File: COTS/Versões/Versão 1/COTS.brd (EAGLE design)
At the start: 76.2 x 79.7 mm, 12 parts

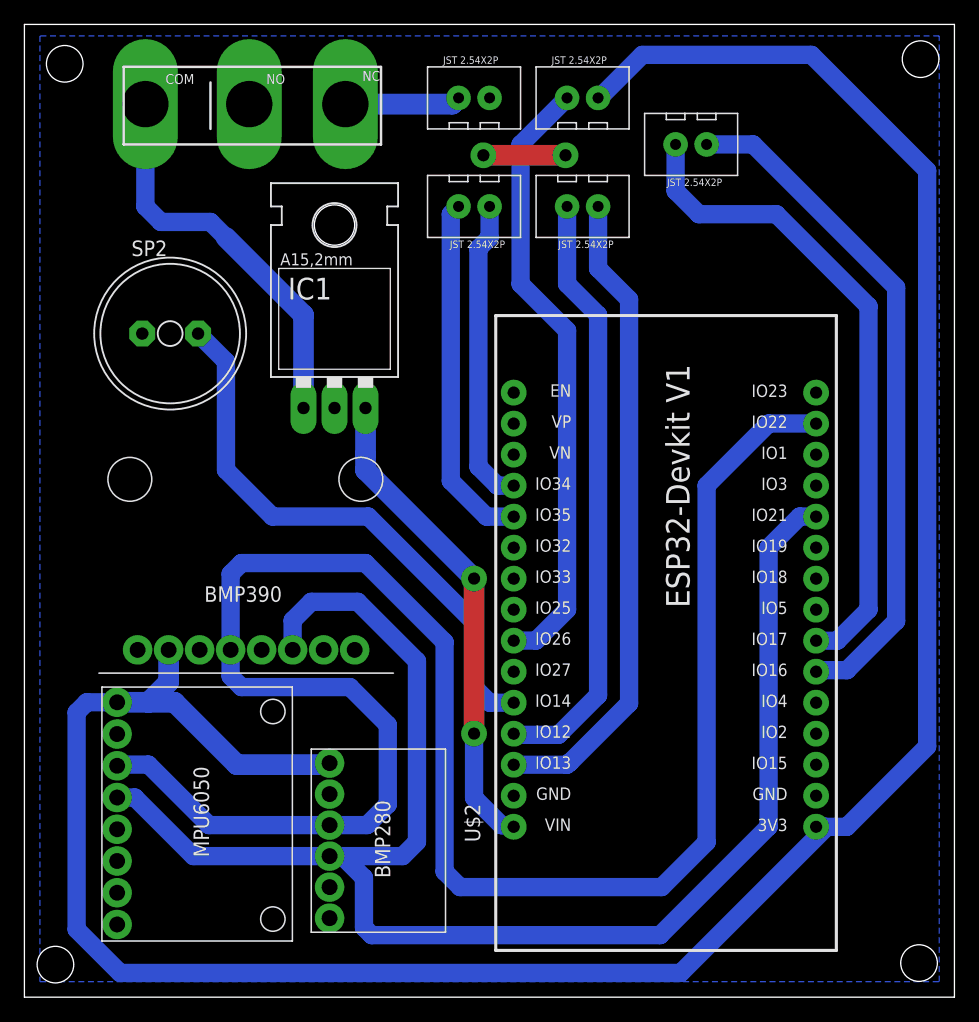
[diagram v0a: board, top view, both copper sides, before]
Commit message: CHORE: colocando  pads ovais
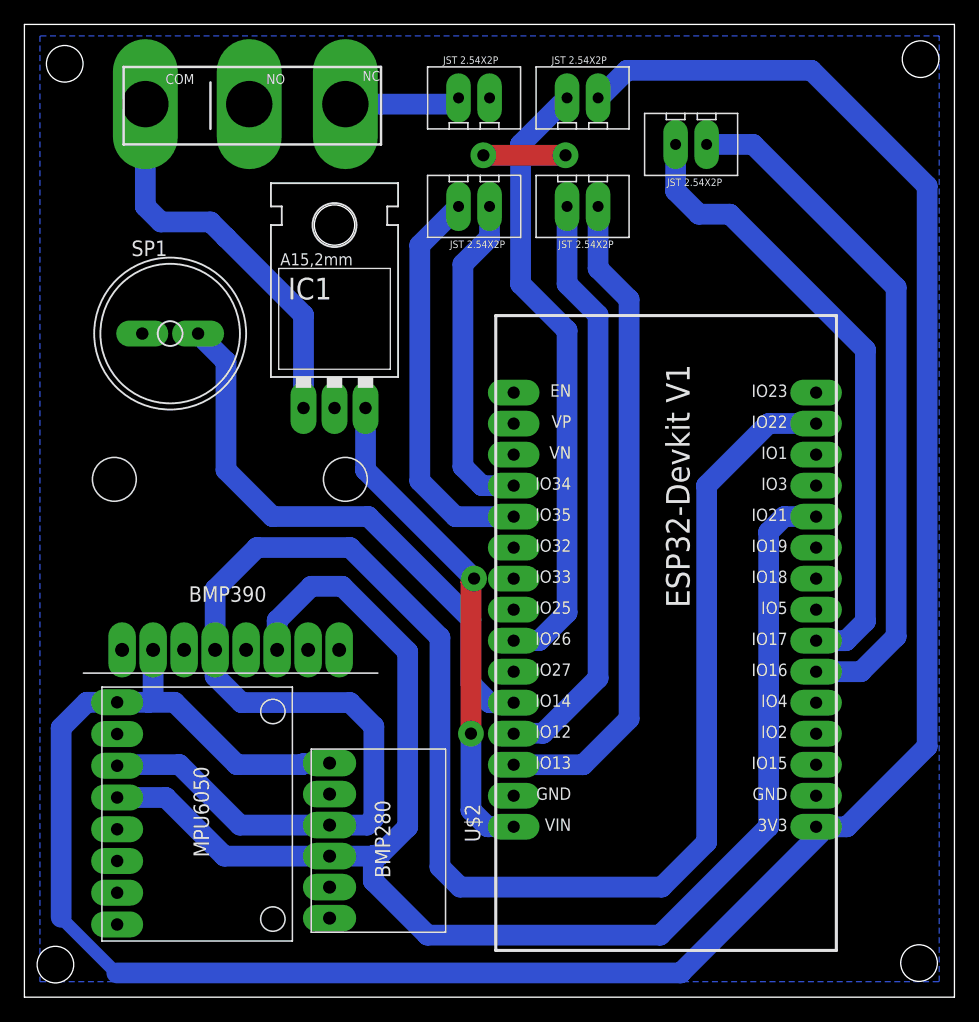
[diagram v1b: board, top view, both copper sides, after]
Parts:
- moved U$3 1.27 mm to (16.5, 36.8)
- renumbered SP2 to SP1
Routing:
- net OPTOACOPLADOR2: track 29.1 -> 32.7 mm
- net SDA: track 128.6 -> 126.1 mm
- net TX2: track 53.7 -> 51.7 mm
- net OPTOACOPLADOR1: track 25.2 -> 27.0 mm
- net SCL: track 157.6 -> 158.7 mm
- net SKIB2: track 49.6 -> 48.5 mm
- net 3V3: track 205.2 -> 204.1 mm
- net 5V: track 39.8 -> 40.8 mm
- net SKIB1: track 53.3 -> 54.0 mm
- net RX2: track 56.0 -> 56.7 mm

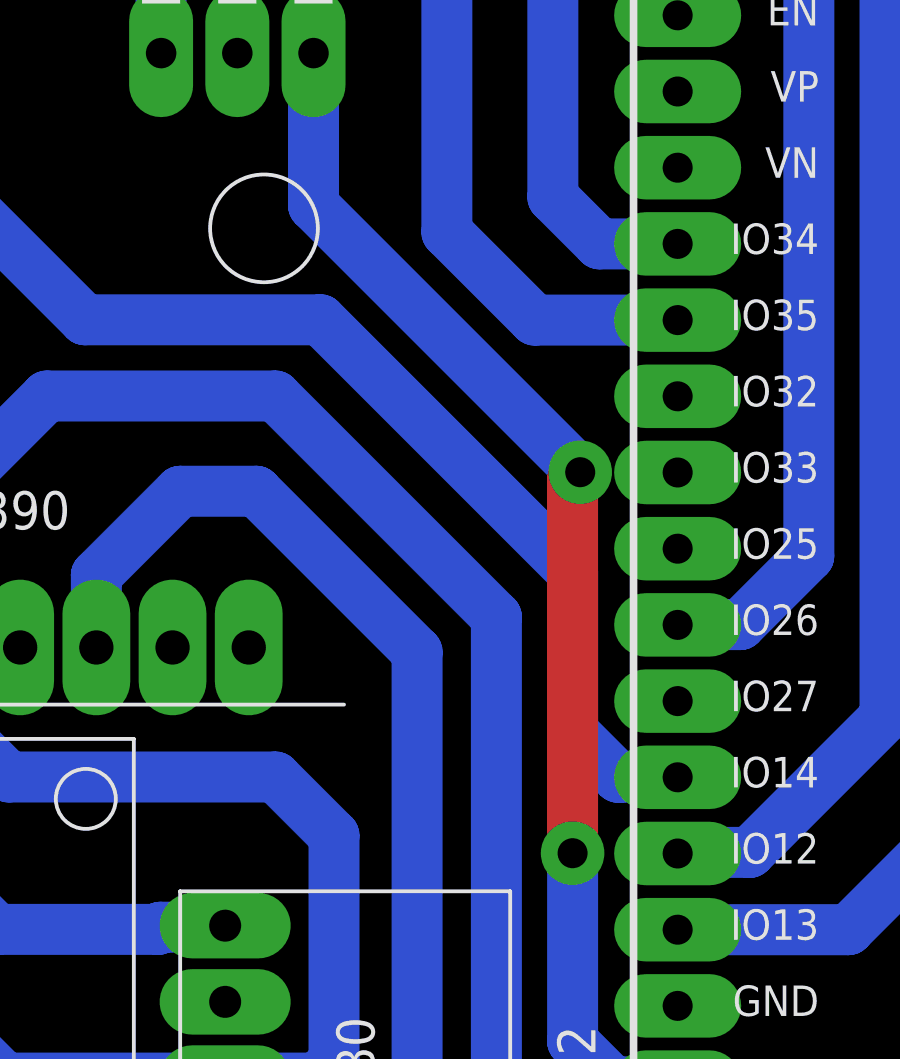
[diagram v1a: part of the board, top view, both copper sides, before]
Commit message: FIX: movendo LoRa para melhor posição
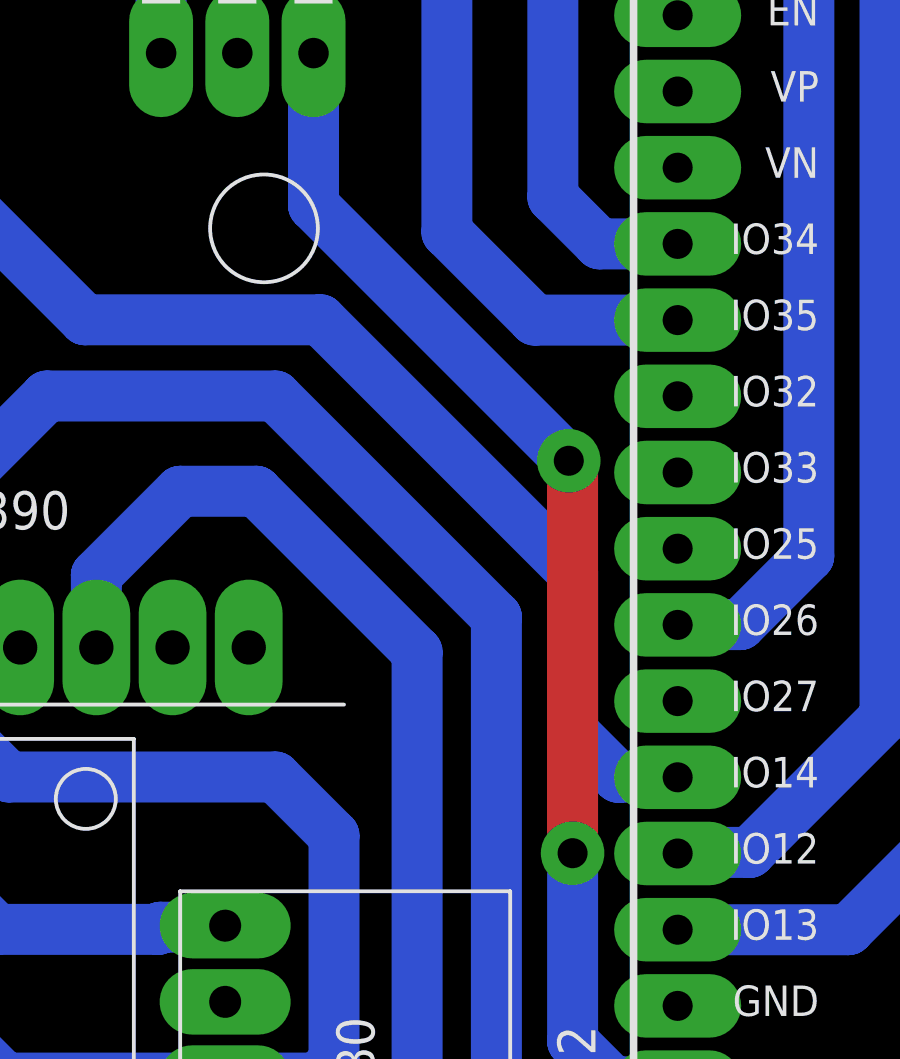
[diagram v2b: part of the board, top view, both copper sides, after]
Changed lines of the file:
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@@
 <elements>
 <element name="U$1" library="CRD" library_urn="urn:adsk.eagle:library:39051337" package="MPU6050_FOOTPRINT" package3d_urn="urn:adsk.eagle:package:39029071/10" override_package3d_urn="urn:adsk.eagle:package:49473311/2" override_package_urn="urn:adsk.eagle:footprint:39029067/6" override_locally_modified="yes" value="MPU6050V1" x="17.78" y="15.24" smashed="yes" rot="R270"/>
-<element name="U$2" library="ESP32-DEVKITV1" library_urn="urn:adsk.eagle:library:44018017" package="ESP32-DEVKITV1" package3d_urn="urn:adsk.eagle:package:44018021/2" value="ESP32DEVKITV1" x="51.308" y="36.83" smashed="yes" rot="R90">
+<element name="U$2" library="ESP32-DEVKITV1" library_urn="urn:adsk.eagle:library:44018017" package="ESP32-DEVKITV1" package3d_urn="urn:adsk.eagle:package:44018021/2" override_package3d_urn="urn:adsk.eagle:package:49887807/2" override_package_urn="urn:adsk.eagle:footprint:49887808/1" value="ESP32DEVKITV1" x="51.308" y="36.83" smashed="yes" rot="R90">
 <attribute name="NAME" x="37.338" y="12.7" size="1.27" layer="21" rot="R90"/>
 </element>
@@
 <element name="U$8" library="CRD" library_urn="urn:adsk.eagle:library:39051337" package="CHAVESS-5GL" package3d_urn="urn:adsk.eagle:package:45208058/14" value="CHAVE_SS-5GL" x="19.05" y="72.39" smashed="yes"/>
 <element name="U$10" library="CRD" library_urn="urn:adsk.eagle:library:39051337" package="BMP280_FOOTPRINT" package3d_urn="urn:adsk.eagle:package:39029072/8" value="BMP280V1" x="31.115" y="12.7" smashed="yes" rot="R270"/>
-<element name="SP1" library="buzzer" package="AL11P" package3d_urn="urn:adsk.eagle:package:5308/1" value="AL11P" x="11.938" y="54.356" smashed="yes">
+<element name="SP1" library="buzzer" package="AL11P" package3d_urn="urn:adsk.eagle:package:5308/1" override_package3d_urn="urn:adsk.eagle:package:49887804/2" override_package_urn="urn:adsk.eagle:footprint:49887805/1" value="AL11P" x="11.938" y="54.356" smashed="yes">
 <attribute name="MF" value="" x="11.938" y="54.356" size="1.778" layer="27" display="off"/>
 <attribute name="MPN" value="" x="11.938" y="54.356" size="1.778" layer="27" display="off"/>
@@
 <wire x1="36.576" y1="21.59" x2="36.576" y2="15.3163875" width="1.7" layer="16"/>
 <via x="36.576" y="21.59" extent="1-16" drill="1"/>
-<wire x1="36.576" y1="34.036" x2="36.83" y2="34.29" width="1.7" layer="1"/>
-<wire x1="36.576" y1="34.036" x2="36.576" y2="21.59" width="1.7" layer="1"/>
-<via x="36.83" y="34.29" extent="1-16" drill="1"/>
-<wire x1="36.83" y1="34.29" x2="27.94" y2="43.18" width="1.7" layer="16"/>
+<wire x1="36.576" y1="34.544" x2="36.449" y2="34.671" width="1.7" layer="1"/>
+<wire x1="36.576" y1="34.544" x2="36.576" y2="21.59" width="1.7" layer="1"/>
+<via x="36.449" y="34.671" extent="1-16" drill="1"/>
+<wire x1="36.449" y1="34.671" x2="27.94" y2="43.18" width="1.7" layer="16"/>
 <wire x1="27.94" y1="43.18" x2="27.94" y2="48.26" width="1.7" layer="16"/>
 <wire x1="36.576" y1="15.3163875" x2="37.9323875" y2="13.96" width="1.7" layer="16"/>
